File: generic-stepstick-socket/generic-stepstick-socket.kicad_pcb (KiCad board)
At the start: 2 copper layers, 3 parts, among them J1 Conn_01x08_Socket, J2 Conn_01x08_Socket, J4 Conn_01x02_Socket

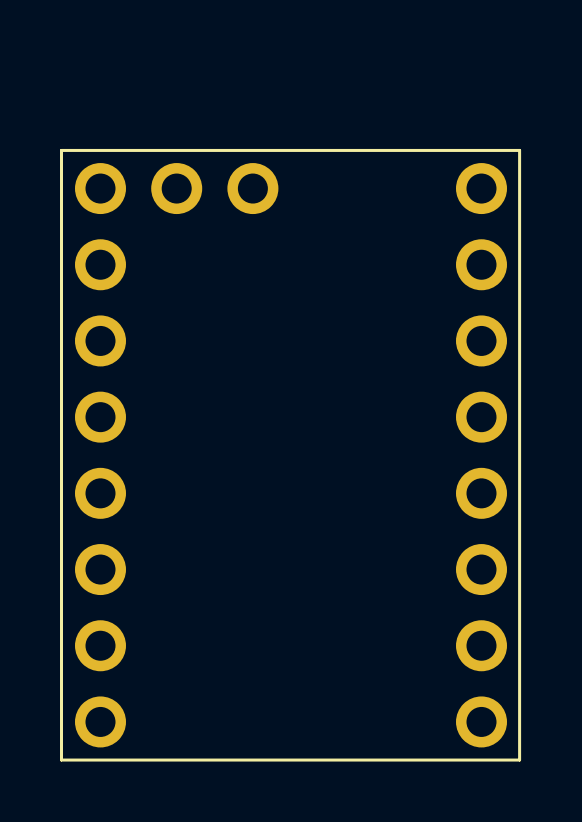
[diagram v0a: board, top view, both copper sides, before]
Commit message: Updated symbols and footprints
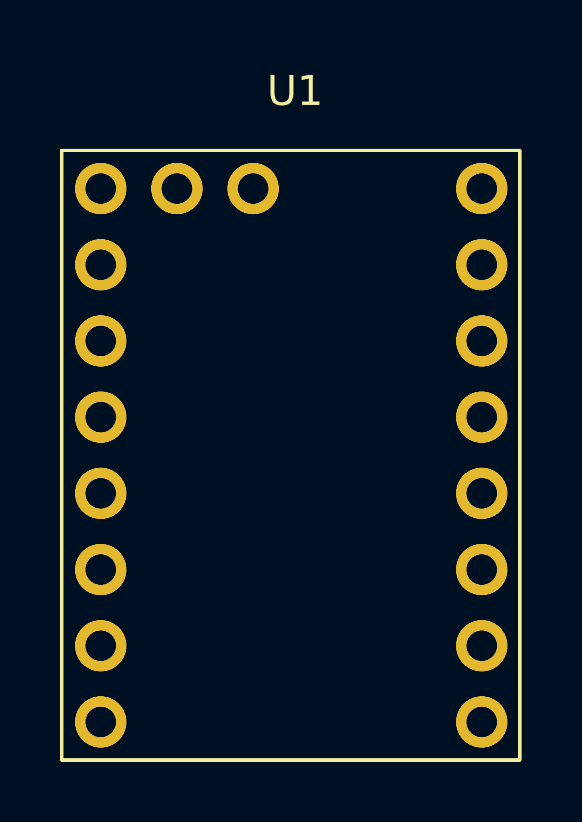
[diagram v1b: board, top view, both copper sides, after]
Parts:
- added U1: ~, generic-stepstick-socket:generic-stepstick-socket, F.Cu at (149.8, 82.1)
